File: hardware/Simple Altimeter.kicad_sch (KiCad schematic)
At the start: 41 parts, among them J1 USB_C_Receptacle_USB2.0, J2 Conn_01x05_Pin, Q1 DMP2240UW, Q2 DMN3067LW, SW1 B3U-1000P, U1 WS4518, U2 BMP280, U3 W25Q16JVUXIQ, U4 STM32F042G6Ux, U5 XB6042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

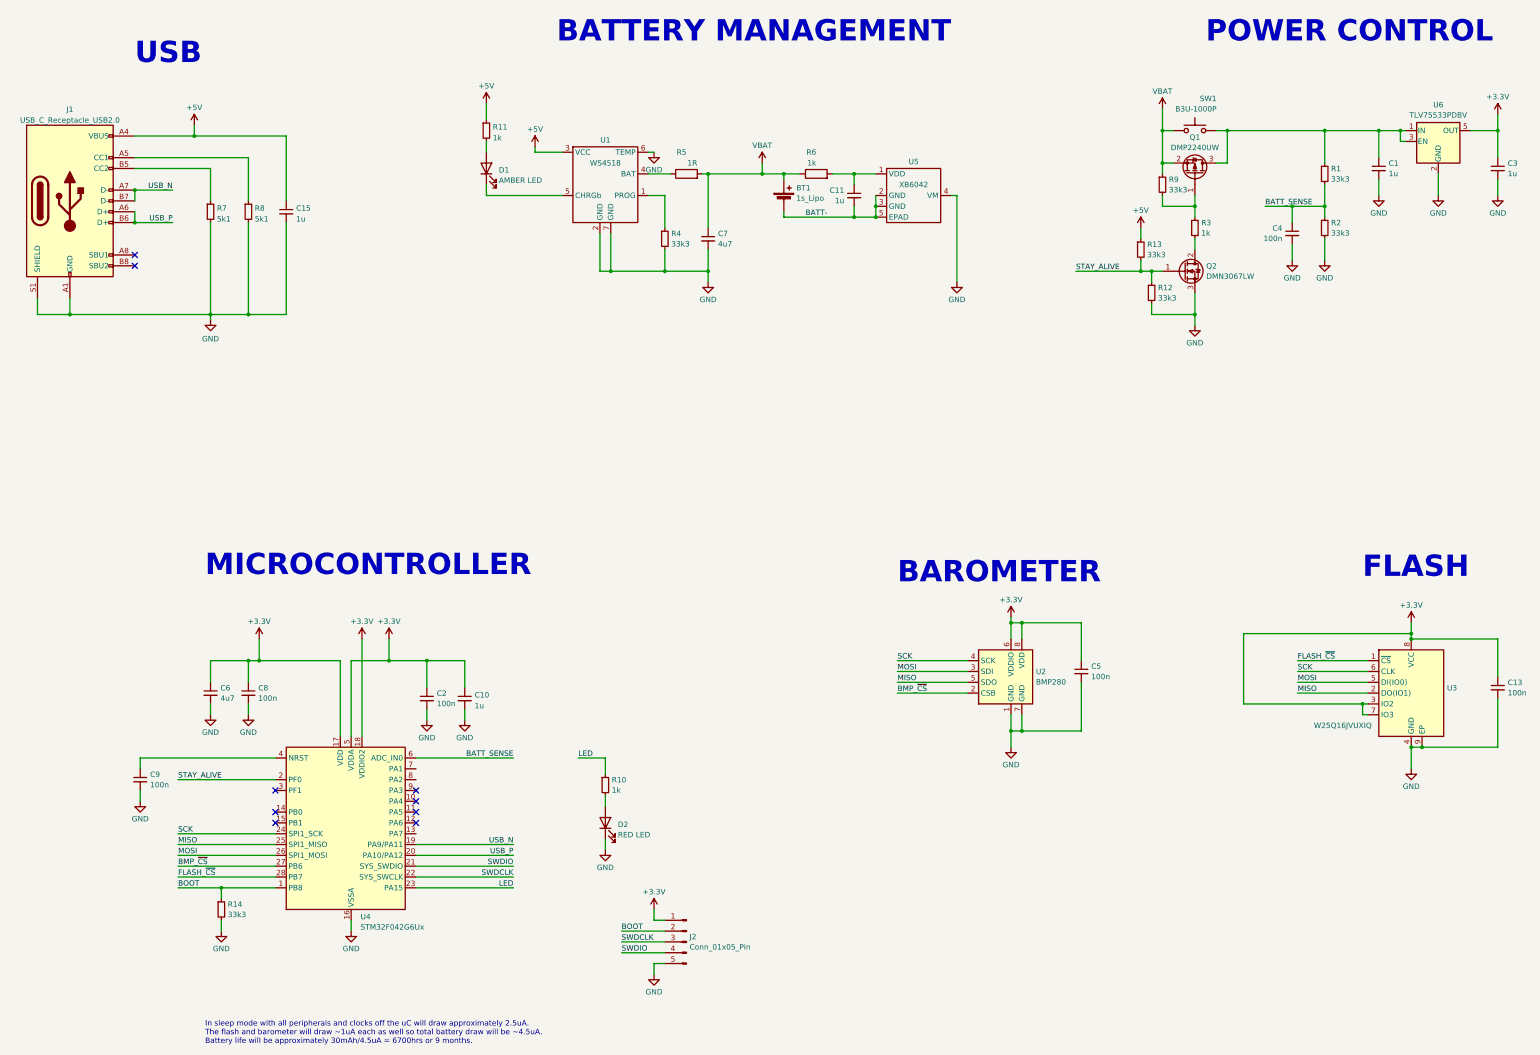
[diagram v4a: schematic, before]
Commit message: Initial commit of STNS01 fork. This will probably become main at some stage in the future.
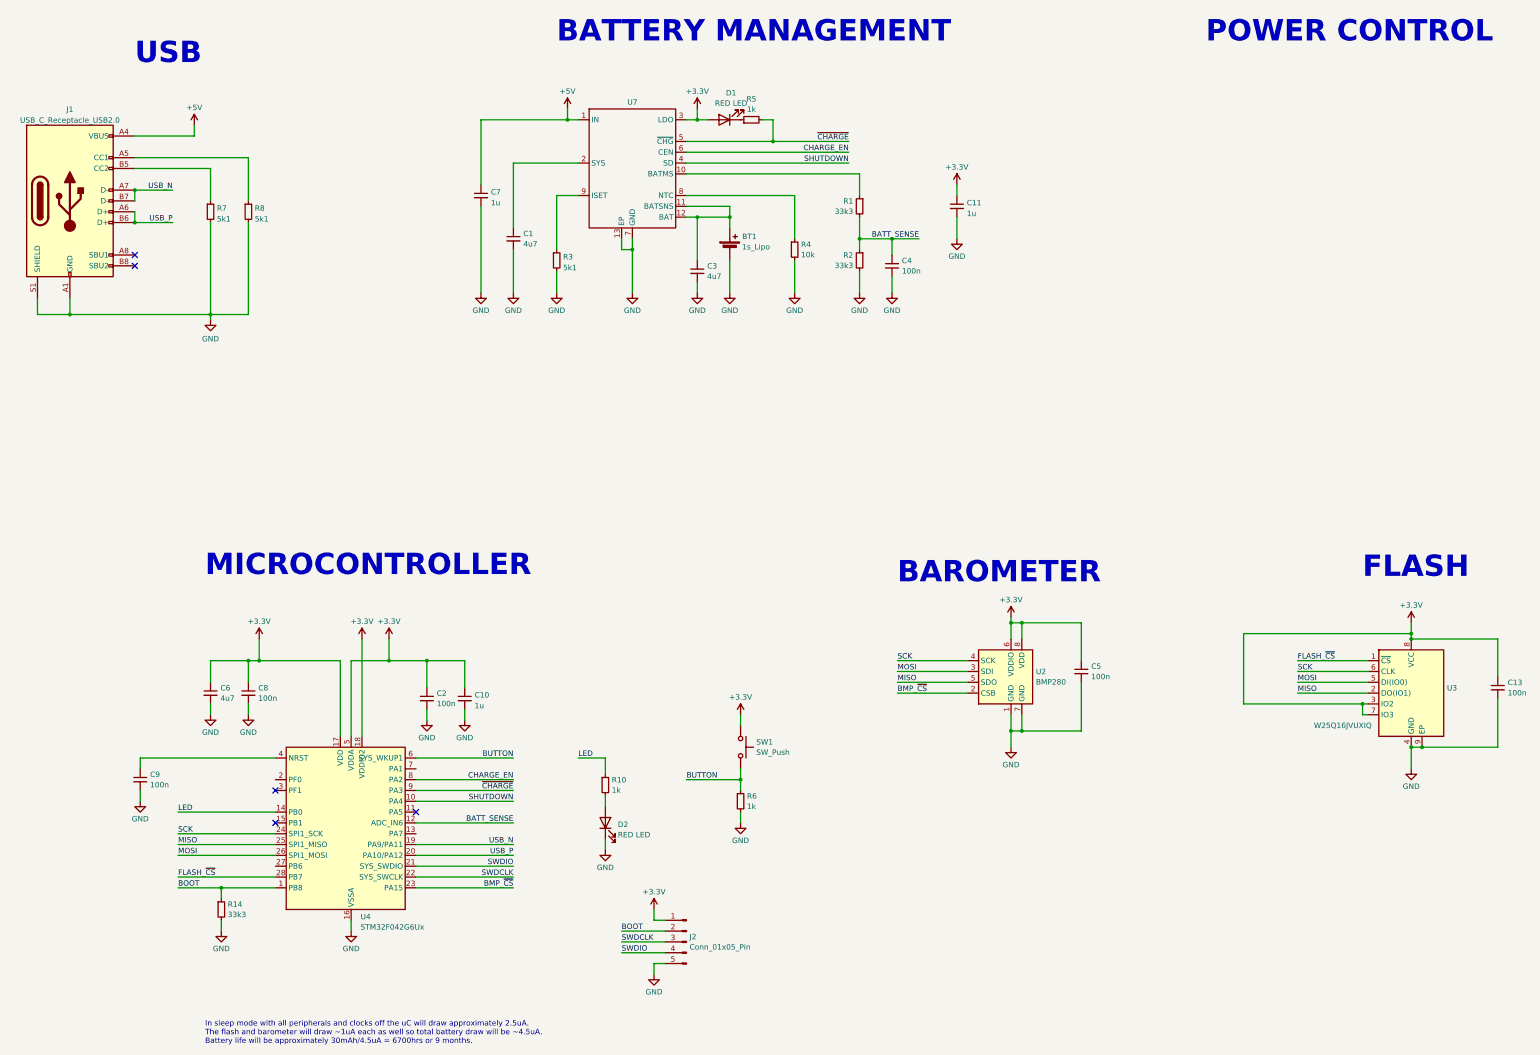
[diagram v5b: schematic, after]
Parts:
- removed C15: 1u, Capacitor_SMD:C_0402_1005Metric, symbol Device:C_Small
- removed Q1: DMP2240UW, Package_TO_SOT_SMD:SOT-323_SC-70, symbol Device:Q_PMOS_GSD
- removed Q2: DMN3067LW, Package_TO_SOT_SMD:SOT-323_SC-70, symbol Device:Q_NMOS_GDS
- removed R11: 1k, Resistor_SMD:R_0402_1005Metric, symbol Device:R_Small
- removed R12, R13, R9: 33k3, Resistor_SMD:R_0402_1005Metric, symbol Device:R_Small
- removed R5: 1R, Resistor_SMD:R_0402_1005Metric, symbol Device:R
- removed R6: 1k, Resistor_SMD:R_0402_1005Metric, symbol Device:R
- removed U1: WS4518, Package_DFN_QFN:DFN-6-1EP_2x2mm_P0.65mm_EP1x1.6mm, symbol My Components:WS4518
- removed U5: XB6042, Package_DFN_QFN:UDFN-4-1EP_1x1mm_P0.65mm_EP0.48x0.48mm, symbol My Components:XB6042
- removed U6: TLV75533PDBV, Package_TO_SOT_SMD:SOT-23-5, symbol Regulator_Linear:TLV75533PDBV
- added R5, R6: 1k, Resistor_SMD:R_0402_1005Metric, symbol Device:R_Small
- added U7: ~, Package_DFN_QFN:DFN-12-1EP_3x3mm_P0.45mm_EP1.66x2.38mm, symbol My Components:SNTS01
- C1, C3: value 1u -> 4u7
- C11: JLC Part Number (none) -> C15849
- C7: value 4u7 -> 1u; JLC Part Number (none) -> C15849
- D1: value AMBER LED -> RED LED
- R3: value 1k -> 5k1
- R4: value 33k3 -> 10k
- SW1: value B3U-1000P -> SW_Push; JLC Part Number C231329 -> (none)
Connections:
- net BATT- is gone; now on net GND: BT1.2 (-), C11.2
- net +3.3V: now also C11.1, D1.2 (A), SW1.2, U7.3 (LDO); no longer C3.1
- net +5V: now also C7.1, U7.1 (IN)
- net BATT_SENSE: now also U4.12 (PA6); no longer U4.6 (PA0)
- net BMP_~{CS}: now also U4.23 (PA15); no longer U4.27 (PB6)
- net GND: now also R3.2, R6.2, U7.13 (EP), U7.7 (GND)
- net LED: now also U4.14 (PB0); no longer U4.23 (PA15)
- net SHUTDOWN: now reaches U4.10 (PA4)
- net SHUTDOWN: now also U7.4 (SD)
- net CHARGE_EN: now reaches U4.8 (PA2)
- net CHARGE_EN: now also U7.6 (CEN)
- net ~{CHARGE}: now reaches U4.9 (PA3)
- net ~{CHARGE}: now also R5.2, U7.5 (~{CHG})
- net at R3.1: now also U7.9 (ISET)
- net at R4.1: now also U7.8 (NTC)
- net at D1.1 (K): now also R5.1
- net STAY_ALIVE: no longer names the net of U4.2 (PF0)
- removed net VBAT: BT1.1 (+), C7.1, SW1.2
- new net: R1.1, U7.10 (BATMS)
- new net: BT1.1 (+), C3.1, U7.11 (BATSNS), U7.12 (BAT)
- new net: C1.1, U7.2 (SYS)
- new net BUTTON: R6.1, SW1.1, U4.6 (PA0)
- no-connect marks 9 -> 5
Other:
- moved on the sheet: BT1, C4, R1, R2

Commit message: Added power off method for debug, and updated operation.md for new hardware. Cleaned up production files.
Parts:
- added J3: Conn_01x02_Pin, Connector_PinHeader_1.27mm:PinHeader_1x02_P1.27mm_Vertical, symbol Connector:Conn_01x02_Pin
- C1: value 4u7 -> 2u2
- C7: value 1u -> 2u2
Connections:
- net +3.3V: now also J3.2 (Pin_2)
- net GND: no longer R2.2
- net SHUTDOWN: now also J3.1 (Pin_1)
- net ~{SENSE_EN}: now reaches U4.7 (PA1)
- net ~{SENSE_EN}: now also R2.2
- no-connect marks 5 -> 8
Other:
- note removed: "POWER CONTROL"
- moved on the sheet: D2, R10

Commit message: fixed footprint for W25Q16JVU
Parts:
- D2: value RED LED -> GREEN LED
- U7: value ~ -> STNS01
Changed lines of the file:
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@@
   (symbol (lib_id "My Components:SNTS01") (at 170.18 60.96 0) (unit 1)
     (in_bom yes) (on_board yes) (dnp no) (fields_autoplaced)
-    (property "Reference" "U7" (at 170.18 46.6669 0)
+    (property "Reference" "U7" (at 170.18 44.2427 0)
       (effects (font (size 1.27 1.27)))
     )
-    (property "Value" "~" (at 170.18 68.58 0)
+    (property "Value" "STNS01" (at 170.18 46.6669 0)
       (effects (font (size 1.27 1.27)))
     )
@@
       (effects (font (size 1.27 1.27)) (justify right))
     )
-    (property "Value" "RED LED" (at 169.291 211.0796 90)
+    (property "Value" "GREEN LED" (at 169.291 211.0796 90)
       (effects (font (size 1.27 1.27)) (justify right))
     )

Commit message: Hardware improvements including a smaller PCB, buzzer and updated file formats to Kicad 8.
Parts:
- removed J2: Conn_01x05_Pin, Connector_PinHeader_1.27mm:PinHeader_1x05_P1.27mm_Vertical, symbol Connector:Conn_01x05_Pin
- removed J3: Conn_01x02_Pin, Connector_PinHeader_1.27mm:PinHeader_1x02_P1.27mm_Vertical, symbol Connector:Conn_01x02_Pin
- added BZ1: Buzzer, My Footprints:Buzzer_0502, symbol Device:Buzzer
- added J2: Conn_01x06_Pin, Connector_PinHeader_1.27mm:PinHeader_1x06_P1.27mm_Vertical, symbol Connector:Conn_01x06_Pin
- added Q1: BC847W, Package_TO_SOT_SMD:SOT-323_SC-70, symbol Transistor_BJT:BC847W
- added R9: 1k, Resistor_SMD:R_0402_1005Metric, symbol Device:R_Small
- BT1: footprint Footprints:Lipo 401010 -> My Footprints:Lipo 401010
- U3: footprint Footprints:Winbond_USON_8_EP_2x3mm -> My Footprints:Winbond_USON_8_EP_2x3mm
- U7: footprint Package_DFN_QFN:DFN-12-1EP_3x3mm_P0.45mm_EP1.66x2.38mm -> Package_DFN_QFN:DFN-12-1EP_3x3mm_P0.45mm_EP1.65x2.38mm
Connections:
- net +3.3V: now also J2.2 (Pin_2)
- net GND: now also J2.6 (Pin_6), Q1.2 (E)
- net SHUTDOWN: now also J2.3 (Pin_3)
- net SWDCLK: now also J2.4 (Pin_4)
- net SWDIO: now also J2.5 (Pin_5)
- net VBAT: now reaches BT1.1 (+), C3.1, U7.11 (BATSNS), U7.12 (BAT)
- net VBAT: now also BZ1.1 (+)
- net BOOT renamed BUZZER/BOOT
- net BUZZER/BOOT: now also J2.1 (Pin_1), R9.1
- new net: BZ1.2 (-), Q1.3 (C)
- new net: Q1.1 (B), R9.2
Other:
- note added: "IO"
- moved on the sheet: D2, R10, R6, SW1
